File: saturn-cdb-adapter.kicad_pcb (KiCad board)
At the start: 2 copper layers, 76.2 x 76.2 mm, 60 parts, among them P1 CONN_02X22, P2 CONN_02X20, P3 CONN_02X20, P4 CONN_02X20, P5 CONN_02X20, U1 SH1, U2 MT28EW_FLASH

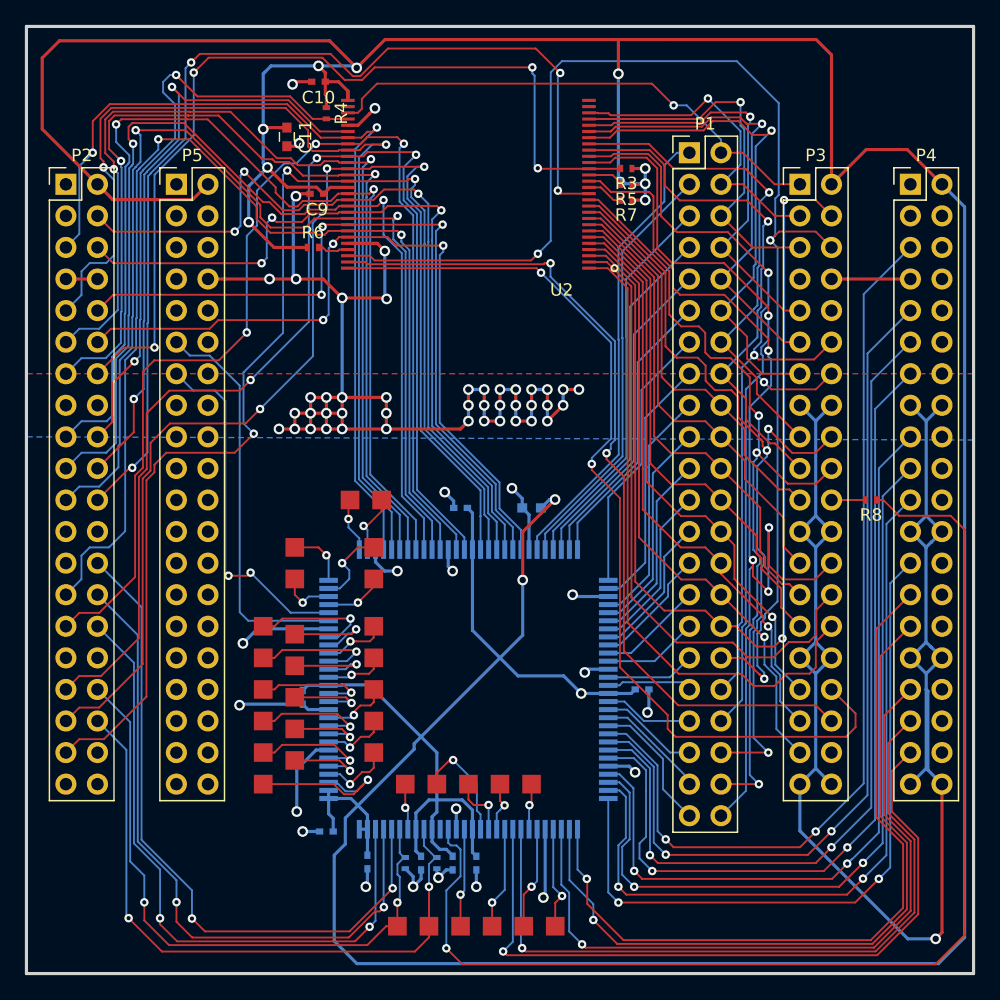
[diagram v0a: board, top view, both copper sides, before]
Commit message: Silkscreen and fab notes fixes
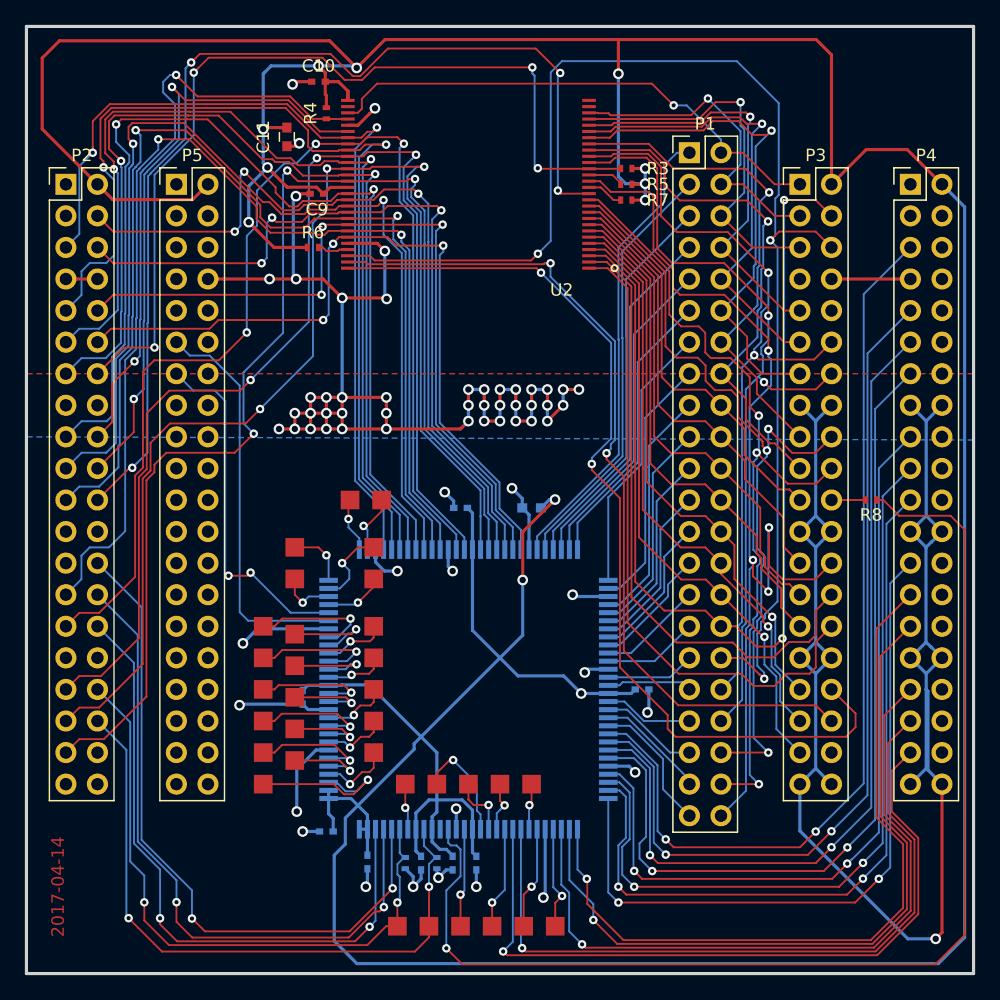
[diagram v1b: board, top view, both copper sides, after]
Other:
- board text added: "2017-04-14"
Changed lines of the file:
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@@
     (area 50.672999 50.672999 127.127001 127.127001)
     (thickness 1.6)
-    (drawings 4)
+    (drawings 5)
     (tracks 1999)
     (zones 0)
@@
     (tags "capacitor 0402")
     (attr smd)
-    (fp_text reference C3 (at 0 1.27 270) (layer B.SilkS)
-      (effects (font (size 1 1) (thickness 0.15)) (justify mirror))
-    )
-    (fp_text value 0.1uF (at 0 -1.27 270) (layer B.Fab)
-      (effects (font (size 1 1) (thickness 0.15)) (justify mirror))
-    )
-    (fp_text user %R (at 0 1.27 270) (layer B.Fab)
+    (fp_text reference C3 (at 2.54 0 270) (layer B.SilkS)
+      (effects (font (size 1 1) (thickness 0.15)) (justify mirror))
+    )
+    (fp_text value 0.1uF (at 6.35 0 270) (layer B.Fab)
+      (effects (font (size 1 1) (thickness 0.15)) (justify mirror))
+    )
+    (fp_text user %R (at 2.54 0 270) (layer B.Fab)
       (effects (font (size 1 1) (thickness 0.15)) (justify mirror))
     )
@@
     (tags "capacitor 0402")
     (attr smd)
-    (fp_text reference C4 (at 0 1.27 270) (layer B.SilkS)
-      (effects (font (size 1 1) (thickness 0.15)) (justify mirror))
-    )
-    (fp_text value 0.1uF (at 0 -1.27 270) (layer B.Fab)
-      (effects (font (size 1 1) (thickness 0.15)) (justify mirror))
-    )
-    (fp_text user %R (at 0 1.27 270) (layer B.Fab)
+    (fp_text reference C4 (at 2.54 0 270) (layer B.SilkS)
+      (effects (font (size 1 1) (thickness 0.15)) (justify mirror))
+    )
+    (fp_text value 0.1uF (at 6.35 0 270) (layer B.Fab)
+      (effects (font (size 1 1) (thickness 0.15)) (justify mirror))
+    )
+    (fp_text user %R (at 2.54 0 270) (layer B.Fab)
       (effects (font (size 1 1) (thickness 0.15)) (justify mirror))
     )
@@
     (tags "capacitor 0402")
     (attr smd)
-    (fp_text reference C5 (at 0 1.27 270) (layer B.SilkS)
-      (effects (font (size 1 1) (thickness 0.15)) (justify mirror))
-    )
-    (fp_text value 0.1uF (at 0 -1.27 270) (layer B.Fab)
-      (effects (font (size 1 1) (thickness 0.15)) (justify mirror))
-    )
-    (fp_text user %R (at 0 1.27 270) (layer B.Fab)
+    (fp_text reference C5 (at 2.54 0 270) (layer B.SilkS)
+      (effects (font (size 1 1) (thickness 0.15)) (justify mirror))
+    )
+    (fp_text value 0.1uF (at 6.35 0 270) (layer B.Fab)
+      (effects (font (size 1 1) (thickness 0.15)) (justify mirror))
+    )
+    (fp_text user %R (at 2.54 0 270) (layer B.Fab)
       (effects (font (size 1 1) (thickness 0.15)) (justify mirror))
     )
@@
     (tags "capacitor 0402")
     (attr smd)
-    (fp_text reference C6 (at 0 1.27 270) (layer B.SilkS)
-      (effects (font (size 1 1) (thickness 0.15)) (justify mirror))
-    )
-    (fp_text value 0.1uF (at 0 -1.27 270) (layer B.Fab)
-      (effects (font (size 1 1) (thickness 0.15)) (justify mirror))
-    )
-    (fp_text user %R (at 0 1.27 270) (layer B.Fab)
+    (fp_text reference C6 (at 2.625 0.127 270) (layer B.SilkS)
+      (effects (font (size 1 1) (thickness 0.15)) (justify mirror))
+    )
+    (fp_text value 0.1uF (at 6.435 0.127 270) (layer B.Fab)
+      (effects (font (size 1 1) (thickness 0.15)) (justify mirror))
+    )
+    (fp_text user %R (at 2.625 0.127 270) (layer B.Fab)
       (effects (font (size 1 1) (thickness 0.15)) (justify mirror))
     )
@@
     (tags "capacitor 0402")
     (attr smd)
-    (fp_text reference C7 (at 0 1.27 180) (layer B.SilkS)
-      (effects (font (size 1 1) (thickness 0.15)) (justify mirror))
-    )
-    (fp_text value 0.1uF (at 0 -1.27 180) (layer B.Fab)
-      (effects (font (size 1 1) (thickness 0.15)) (justify mirror))
-    )
-    (fp_text user %R (at 0 1.27 180) (layer B.Fab)
+    (fp_text reference C7 (at 0 -1.27 180) (layer B.SilkS)
+      (effects (font (size 1 1) (thickness 0.15)) (justify mirror))
+    )
+    (fp_text value 0.1uF (at 0.635 1.27 180) (layer B.Fab)
+      (effects (font (size 1 1) (thickness 0.15)) (justify mirror))
+    )
+    (fp_text user %R (at 0 -1.27 180) (layer B.Fab)
       (effects (font (size 1 1) (thickness 0.15)) (justify mirror))
     )
@@
     (tags "capacitor 0402")
     (attr smd)
-    (fp_text reference C10 (at 0 -1.27 180) (layer F.SilkS)
-      (effects (font (size 1 1) (thickness 0.15)))
-    )
-    (fp_text value 0.1uF (at 0 1.27 180) (layer F.Fab)
-      (effects (font (size 1 1) (thickness 0.15)))
-    )
-    (fp_text user %R (at 0 -1.27 180) (layer F.Fab)
+    (fp_text reference C10 (at 0 1.27 180) (layer F.SilkS)
+      (effects (font (size 1 1) (thickness 0.15)))
+    )
+    (fp_text value 0.1uF (at 3.175 0 180) (layer F.Fab)
+      (effects (font (size 1 1) (thickness 0.15)))
+    )
+    (fp_text user %R (at 0 1.27 180) (layer F.Fab)
       (effects (font (size 1 1) (thickness 0.15)))
     )
@@
     (tags "capacitor 0603")
     (attr smd)
-    (fp_text reference C11 (at 0 -1.5 270) (layer F.SilkS)
-      (effects (font (size 1 1) (thickness 0.15)))
-    )
-    (fp_text value 1uF (at 0 1.5 270) (layer F.Fab)
-      (effects (font (size 1 1) (thickness 0.15)))
-    )
-    (fp_text user %R (at 0 -1.5 270) (layer F.Fab)
+    (fp_text reference C11 (at 0 1.905 450) (layer F.SilkS)
+      (effects (font (size 1 1) (thickness 0.15)))
+    )
+    (fp_text value 1uF (at 0.635 -1.905 450) (layer F.Fab)
+      (effects (font (size 1 1) (thickness 0.15)))
+    )
+    (fp_text user %R (at 0 1.905 450) (layer F.Fab)
       (effects (font (size 1 1) (thickness 0.15)))
     )
@@
     (tags "resistor 0402")
     (attr smd)
-    (fp_text reference R1 (at 0 1.2 270) (layer B.SilkS)
-      (effects (font (size 1 1) (thickness 0.15)) (justify mirror))
-    )
-    (fp_text value 10k (at 0 -1.25 270) (layer B.Fab)
-      (effects (font (size 1 1) (thickness 0.15)) (justify mirror))
-    )
-    (fp_text user %R (at 0 1.2 270) (layer B.Fab)
+    (fp_text reference R1 (at 2.54 0 270) (layer B.SilkS)
+      (effects (font (size 1 1) (thickness 0.15)) (justify mirror))
+    )
+    (fp_text value 10k (at 5.715 0 270) (layer B.Fab)
+      (effects (font (size 1 1) (thickness 0.15)) (justify mirror))
+    )
+    (fp_text user %R (at 2.54 0 270) (layer B.Fab)
       (effects (font (size 1 1) (thickness 0.15)) (justify mirror))
     )
@@
     (tags "resistor 0402")
     (attr smd)
-    (fp_text reference R2 (at 0 1.2 270) (layer B.SilkS)
-      (effects (font (size 1 1) (thickness 0.15)) (justify mirror))
-    )
-    (fp_text value 10k (at 0 -1.25 270) (layer B.Fab)
-      (effects (font (size 1 1) (thickness 0.15)) (justify mirror))
-    )
-    (fp_text user %R (at 0 1.2 270) (layer B.Fab)
+    (fp_text reference R2 (at 2.54 0 270) (layer B.SilkS)
+      (effects (font (size 1 1) (thickness 0.15)) (justify mirror))
+    )
+    (fp_text value 10k (at 5.715 0 270) (layer B.Fab)
+      (effects (font (size 1 1) (thickness 0.15)) (justify mirror))
+    )
+    (fp_text user %R (at 2.54 0 270) (layer B.Fab)
       (effects (font (size 1 1) (thickness 0.15)) (justify mirror))
     )
@@
     (tags "resistor 0402")
     (attr smd)
-    (fp_text reference R3 (at 0 -1.2 180) (layer F.SilkS)
-      (effects (font (size 1 1) (thickness 0.15)))
-    )
-    (fp_text value 10k (at 0 1.25 180) (layer F.Fab)
-      (effects (font (size 1 1) (thickness 0.15)))
-    )
-    (fp_text user %R (at 0 -1.2 180) (layer F.Fab)
+    (fp_text reference R3 (at -2.54 0 180) (layer F.SilkS)
+      (effects (font (size 1 1) (thickness 0.15)))
+    )
+    (fp_text value 10k (at 1.905 0 180) (layer F.Fab)
+      (effects (font (size 1 1) (thickness 0.15)))
+    )
+    (fp_text user %R (at -2.54 0 180) (layer F.Fab)
       (effects (font (size 1 1) (thickness 0.15)))
     )
@@
     (tags "resistor 0402")
     (attr smd)
-    (fp_text reference R4 (at 0 -1.2 270) (layer F.SilkS)
-      (effects (font (size 1 1) (thickness 0.15)))
-    )
-    (fp_text value 10k (at 0 1.25 270) (layer F.Fab)
-      (effects (font (size 1 1) (thickness 0.15)))
-    )
-    (fp_text user %R (at 0 -1.2 270) (layer F.Fab)
+    (fp_text reference R4 (at 0 1.27 270) (layer F.SilkS)
+      (effects (font (size 1 1) (thickness 0.15)))
+    )
+    (fp_text value 10k (at 0 -1.27 450) (layer F.Fab)
+      (effects (font (size 1 1) (thickness 0.15)))
+    )
+    (fp_text user %R (at 0 1.27 450) (layer F.Fab)
       (effects (font (size 1 1) (thickness 0.15)))
     )
@@
     (tags "resistor 0402")
     (attr smd)
-    (fp_text reference R5 (at 0 -1.2 180) (layer F.SilkS)
-      (effects (font (size 1 1) (thickness 0.15)))
-    )
-    (fp_text value 0 (at 0 1.25 180) (layer F.Fab)
-      (effects (font (size 1 1) (thickness 0.15)))
-    )
-    (fp_text user %R (at 0 -1.2 180) (layer F.Fab)
+    (fp_text reference R5 (at -2.54 0 180) (layer F.SilkS)
+      (effects (font (size 1 1) (thickness 0.15)))
+    )
+    (fp_text value 0 (at 1.905 0 180) (layer F.Fab)
+      (effects (font (size 1 1) (thickness 0.15)))
+    )
+    (fp_text user %R (at -2.54 0 180) (layer F.Fab)
       (effects (font (size 1 1) (thickness 0.15)))
     )
@@
     (tags "resistor 0402")
     (attr smd)
-    (fp_text reference R7 (at 0 -1.2 180) (layer F.SilkS)
-      (effects (font (size 1 1) (thickness 0.15)))
-    )
-    (fp_text value 0 (at 0 1.25 180) (layer F.Fab)
-      (effects (font (size 1 1) (thickness 0.15)))
-    )
-    (fp_text user %R (at 0 -1.2 180) (layer F.Fab)
+    (fp_text reference R7 (at -2.54 0 180) (layer F.SilkS)
+      (effects (font (size 1 1) (thickness 0.15)))
+    )
+    (fp_text value 0 (at 1.905 0 180) (layer F.Fab)
+      (effects (font (size 1 1) (thickness 0.15)))
+    )
+    (fp_text user %R (at -2.54 0 180) (layer F.Fab)
       (effects (font (size 1 1) (thickness 0.15)))
     )
@@
       (net 163 "Net-(U1-Pad94)"))
   )
+  (gr_text 2017-04-14 (at 53.34 120.015 90) (layer F.Cu)
+    (effects (font (size 1.016 1.016) (thickness 0.254)))
+  )
   (gr_line (start 127 50.8) (end 50.8 50.8) (layer Edge.Cuts) (width 0.254))

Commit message: Final OCD fixes
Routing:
- net ~FLASH_OE: track 49.3 -> 51.0 mm
- net ~FLASH_CE: track 48.1 -> 49.9 mm
- net ~FLASH_WE: track 83.0 -> 84.8 mm
- net CPU_TX: track 28.7 -> 30.3 mm
- net AD9: track 97.9 -> 99.2 mm
- net AD10: track 99.7 -> 101.0 mm
- net FLASH_A19: track 65.5 -> 66.6 mm
- net +3V3: track 402.6 -> 403.5 mm
- net FLASH_A23: track 52.4 -> 51.7 mm
- net AD8: track 93.9 -> 94.6 mm
- net AD11: track 102.5 -> 103.2 mm
- net FLASH_A18: track 65.1 -> 65.7 mm
